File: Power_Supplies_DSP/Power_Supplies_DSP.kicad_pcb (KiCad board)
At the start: 4 copper layers, 149.3 x 91.8 mm, 54 parts, among them J22 USB_C_Receptacle_USB2.0, J28 PINHD_1x2_Female, J34 PINHD_1x1_Female, J35 PINHD_1x1_Female, J37 PINHD_1x3_Female, J41 PINHD_1x10_Female, J8 FTSH-110-01-F-DV-K, U12 XU316-1024-TQ128-I24, U13 Si5351A-B-GT, U14 W25Q64JVSSIQ (FLASH MEMORY), U37 PEC11R-4030F-N0024, X1 FA-238 24.0000MB-C0 (CRYSTAL), X2 FA-238 24.0000MB-C0

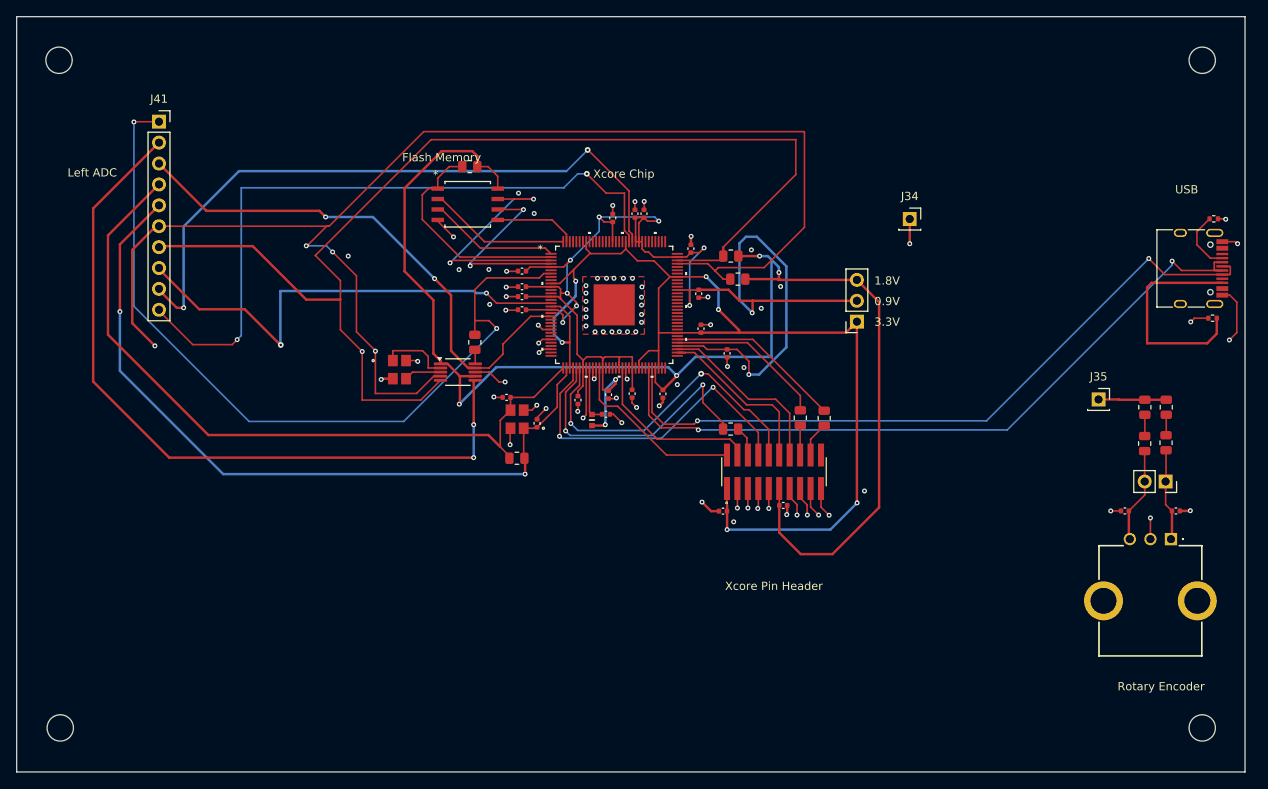
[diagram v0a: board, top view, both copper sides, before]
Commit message: mcu PCB
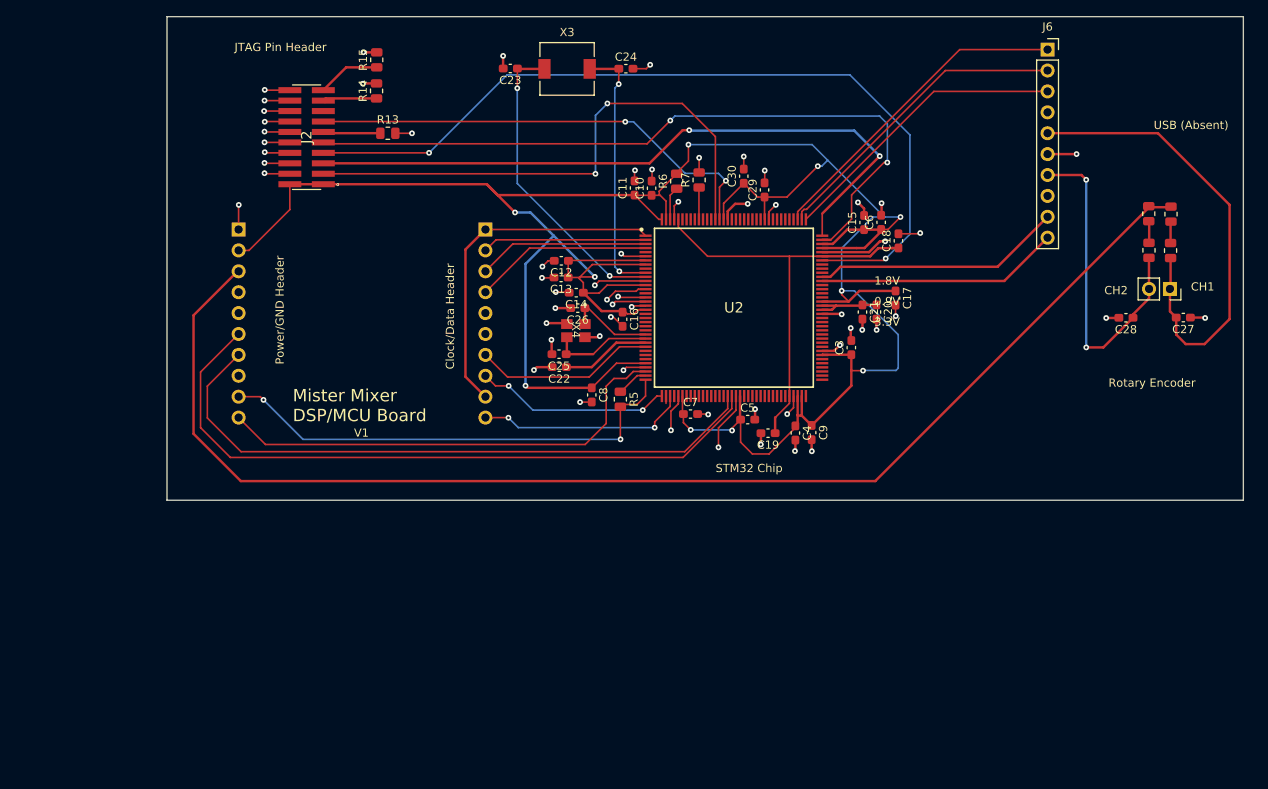
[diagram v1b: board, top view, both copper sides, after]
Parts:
- removed C202, C203, C204, C205, C207, C208, C209, C210, C211, C212, C213, C214, C215, C216, C217, C218: 100nF, Capacitor_SMD:C_0402_1005Metric
- removed C206: 2.2uF, Capacitor_SMD:C_0402_1005Metric
- removed C232: 1uF, Capacitor_SMD:C_0402_1005Metric
- removed C49, C50: 18pF, Capacitor_SMD:C_0402_1005Metric
- removed FL1: BLM18AG601SZ1D, SamacSys_Parts:BLM18SP221SN1B
- removed H1, H2, H3, H4: MountingHole_M3, MountingHole:MountingHole_3.2mm_M3
- removed J22: USB_C_Receptacle_USB2.0, Connector_USB:USB_C_Receptacle_HRO_TYPE-C-31-M-12
- removed J34, J35: PINHD_1x1_Female, Connector_PinSocket_2.54mm:PinSocket_1x01_P2.54mm_Vertical
- removed J37: PINHD_1x3_Female, Connector_PinSocket_2.54mm:PinSocket_1x03_P2.54mm_Vertical
- removed J41: PINHD_1x10_Female, Connector_PinSocket_2.54mm:PinSocket_1x10_P2.54mm_Vertical
- removed J8: FTSH-110-01-F-DV-K, SamacSys_Parts:FTSH-110-XX-YYY-DV-K
- removed R164: 0, Resistor_SMD:R_0805_2012Metric
- removed R165, R166: 43, Resistor_SMD:R_0805_2012Metric
- removed R174, R179: 5k1, Resistor_SMD:R_0402_1005Metric
- removed R34: 10K, Resistor_SMD:R_0805_2012Metric
- removed R35: 33, Resistor_SMD:R_0805_2012Metric
- removed R36: 1M, Resistor_SMD:R_0805_2012Metric
- removed R72, R73: 4.7K, Resistor_SMD:R_0805_2012Metric
- removed U12: XU316-1024-TQ128-I24, SamacSys_Parts:TQFP128_196X196_XMO
- removed U13: Si5351A-B-GT, Package_SO:MSOP-10_3x3mm_P0.5mm
- removed U14: W25Q64JVSSIQ (FLASH MEMORY), SamacSys_Parts:SOIC-8_5P28X5P28_WIN
- removed U37: PEC11R-4030F-N0024, SamacSys_Parts:PEC11R4030FN0024
- removed X1: FA-238 24.0000MB-C0 (CRYSTAL), SamacSys_Parts:FA-238_EPS
- removed X2: FA-238 24.0000MB-C0, SamacSys_Parts:FA-238_EPS
- added C10: 100nF, Capacitor_SMD:C_0603_1608Metric_Pad1.08x0.95mm_HandSolder, F.Cu at (201.4, 136.8)
- added C11: 100nF, Capacitor_SMD:C_0603_1608Metric_Pad1.08x0.95mm_HandSolder, F.Cu at (199.3, 136.7)
- added C12: 100nF, Capacitor_SMD:C_0603_1608Metric_Pad1.08x0.95mm_HandSolder, F.Cu at (190.4, 145.6)
- added C13: 100nF, Capacitor_SMD:C_0603_1608Metric_Pad1.08x0.95mm_HandSolder, F.Cu at (190.4, 147.6)
- added C14: 4.7 uF, Capacitor_SMD:C_0603_1608Metric_Pad1.08x0.95mm_HandSolder, F.Cu at (192.2, 149.4)
- added C15: 100nF, Capacitor_SMD:C_0603_1608Metric_Pad1.08x0.95mm_HandSolder, F.Cu at (227.2, 140.9)
- added C16: 100nF, Capacitor_SMD:C_0603_1608Metric_Pad1.08x0.95mm_HandSolder, F.Cu at (197.8, 152.7)
- added C17: 4.7uF, Capacitor_SMD:C_0603_1608Metric_Pad1.08x0.95mm_HandSolder, F.Cu at (231.0, 150.1)
- added C18: 2.2uF, Capacitor_SMD:C_0603_1608Metric_Pad1.08x0.95mm_HandSolder, F.Cu at (231.4, 143.2)
- added C19: 2.2uF, Capacitor_SMD:C_0603_1608Metric_Pad1.08x0.95mm_HandSolder, F.Cu at (215.5, 166.5)
- added C20: 1uF, Capacitor_SMD:C_0603_1608Metric_Pad1.08x0.95mm_HandSolder, F.Cu at (228.7, 151.8)
- added C21: 100nF, Capacitor_SMD:C_0603_1608Metric_Pad1.08x0.95mm_HandSolder, F.Cu at (227.0, 151.8)
- added C22: 100nF, Capacitor_SMD:C_0603_1608Metric_Pad1.08x0.95mm_HandSolder, F.Cu at (190.2, 158.5)
- added C23: 12pF, Capacitor_SMD:C_0603_1608Metric_Pad1.08x0.95mm_HandSolder, F.Cu at (184.2, 122.2)
- added C24: 12pF, Capacitor_SMD:C_0603_1608Metric_Pad1.08x0.95mm_HandSolder, F.Cu at (198.2, 122.2)
- added C25: 10pF, Capacitor_SMD:C_0603_1608Metric_Pad1.08x0.95mm_HandSolder, F.Cu at (190.1, 156.9)
- added C26: 10pF, Capacitor_SMD:C_0603_1608Metric_Pad1.08x0.95mm_HandSolder, F.Cu at (192.4, 151.3)
- added C29: 100nF, Capacitor_SMD:C_0603_1608Metric_Pad1.08x0.95mm_HandSolder, F.Cu at (215.1, 137.0)
- added C3: 100nF, Capacitor_SMD:C_0603_1608Metric_Pad1.08x0.95mm_HandSolder, F.Cu at (225.7, 156.1)
- added C30: 100nF, Capacitor_SMD:C_0603_1608Metric_Pad1.08x0.95mm_HandSolder, F.Cu at (212.6, 135.3)
- added C4: 100nF, Capacitor_SMD:C_0603_1608Metric_Pad1.08x0.95mm_HandSolder, F.Cu at (218.8, 166.5)
- added C5: 100nF, Capacitor_SMD:C_0603_1608Metric_Pad1.08x0.95mm_HandSolder, F.Cu at (213.1, 164.9)
- added C6: 100nF, Capacitor_SMD:C_0603_1608Metric_Pad1.08x0.95mm_HandSolder, F.Cu at (229.3, 140.9)
- added C7: 100nF, Capacitor_SMD:C_0603_1608Metric_Pad1.08x0.95mm_HandSolder, F.Cu at (206.1, 164.2)
- added C8: 100nF, Capacitor_SMD:C_0603_1608Metric_Pad1.08x0.95mm_HandSolder, F.Cu at (194.1, 161.9)
- added C9: 100nF, Capacitor_SMD:C_0603_1608Metric_Pad1.08x0.95mm_HandSolder, F.Cu at (220.8, 166.4)
- added J1: PINHD_1x10_Male, Connector_PinHeader_2.54mm:PinHeader_1x10_P2.54mm_Vertical, B.Cu at (151.2, 141.8)
- added J2: SBH11-PBPC-D10-ST-BK, SamacSys_Parts:FTSH-110-XX-YYY-DV-K, F.Cu at (159.4, 130.6)
- added J4: PINHD_1x10_Male, Connector_PinHeader_2.54mm:PinHeader_1x10_P2.54mm_Vertical, B.Cu at (181.2, 141.8)
- added J6: PINHD_1x10_Female, Connector_PinSocket_2.54mm:PinSocket_1x10_P2.54mm_Vertical, F.Cu at (249.5, 119.9)
- added R13: 10k, Resistor_SMD:R_0805_2012Metric, F.Cu at (169.3, 130.1)
- added R14: 10k, Resistor_SMD:R_0805_2012Metric, F.Cu at (167.9, 124.9)
- added R15: 10k, Resistor_SMD:R_0805_2012Metric, F.Cu at (168.0, 121.2)
- added R5: 47, Resistor_SMD:R_0805_2012Metric, F.Cu at (197.6, 162.4)
- added R6: 10k, Resistor_SMD:R_0805_2012Metric, F.Cu at (204.4, 135.9)
- added R7: 10k, Resistor_SMD:R_0805_2012Metric, F.Cu at (207.2, 135.8)
- added U2: STM32H755ZIT6, SamacSys_Parts:QFP50P2200X2200X160-144N, F.Cu at (211.4, 151.3)
- added X3: NX3215SA-32.768K, Inductor_SMD:L_6.3x6.3_H3, F.Cu at (191.1, 122.2)
- added X4: NX2016SA-32MHZ, SamacSys_Parts:FA-238_EPS, F.Cu at (192.2, 154.1)
- C27: renamed from C235; footprint Capacitor_SMD:C_0402_1005Metric -> Capacitor_SMD:C_0603_1608Metric_Pad1.08x0.95mm_HandSolder
- C28: renamed from C234; footprint Capacitor_SMD:C_0402_1005Metric -> Capacitor_SMD:C_0603_1608Metric_Pad1.08x0.95mm_HandSolder
- moved R10 27.9 mm to (261.8, 139.8)
- moved C27 24.6 mm to (266.0, 152.5)
- moved C28 24.3 mm to (259.0, 152.5)
- moved R8 23.7 mm to (264.5, 139.9)
- moved R11 23.5 mm to (261.8, 144.3)
- moved J5 23.4 mm to (264.4, 149.0)
- moved R9 19.1 mm to (264.4, 144.3)
- renumbered J28 to J5, R178 to R10, R177 to R11, R176 to R8, R175 to R9
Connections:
- C27 pad 1: Net-(U37-CHANNEL_2) -> GND
- C27 pad 2: GND -> CHANNEL_1
- C28 pad 1: GND -> CHANNEL_2
- C28 pad 2: Net-(U37-CHANNEL_1) -> GND
- J5 pad 1: Net-(U37-CHANNEL_1) -> CHANNEL_1
- J5 pad 2: Net-(U37-CHANNEL_2) -> CHANNEL_2
- R10 pad 1: Net-(R176-Pad2) -> 5V
- R10 pad 2: Net-(U37-CHANNEL_2) -> Net-(R10-Pad2)
- R11 pad 1: Net-(R175-Pad2) -> Net-(R10-Pad2)
- R11 pad 2: Net-(U37-CHANNEL_1) -> CHANNEL_2
- R8 pad 2: Net-(R176-Pad2) -> Net-(R8-Pad2)
- R9 pad 1: 5V -> Net-(R8-Pad2)
- R9 pad 2: Net-(R175-Pad2) -> CHANNEL_1
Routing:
- net 0.9V: track 185.3 -> 0.00 mm, vias 12 -> 0
- net SCL: track 167.2 -> 0.00 mm, vias 4 -> 0
- net 3.3V: track 177.3 -> 328.5 mm, vias 4 -> 10
- net 5V: track 8.24 -> 157.0 mm
- net SDA: track 144.1 -> 0.00 mm, vias 1 -> 0
- net 1.8V: track 137.6 -> 0.00 mm, vias 6 -> 0
- net SWDIO: track 0.00 -> 102.3 mm, vias 0 -> 2
- net MCLK: track 98.7 -> 0.00 mm, vias 2 -> 0
- net XIN: track 92.4 -> 0.00 mm, vias 2 -> 0
- net BCK: track 91.9 -> 0.00 mm, vias 2 -> 0
- net XOUT: track 90.6 -> 0.00 mm
- net SWCLK: track 0.00 -> 88.6 mm, vias 0 -> 2
- net USB_DN: track 88.4 -> 0.00 mm, vias 2 -> 0
- net USB_DP: track 87.3 -> 0.00 mm, vias 2 -> 0
- net DATA_OUT_2: track 84.9 -> 0.00 mm, vias 2 -> 0
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- removed copper zone on F.Cu, net GND
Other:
- board size 149.3 x 91.8 mm -> 130.8 x 58.8 mm
- board text added: "CH1"
- board text added: "CH2"
- board text added: "Clock/Data Header"
- board text added: "JTAG Pin Header"
- board text added: "Mister Mixer DSP/MCU Board"
- board text added: "Power/GND Header"
- board text added: "STM32 Chip"
- board text added: "USB (Absent)"
- board text added: "V1"
- board text removed: "Flash Memory"
- board text removed: "Left ADC"
- board text removed: "USB"
- board text removed: "Xcore Chip"
- board text removed: "Xcore Pin Header"

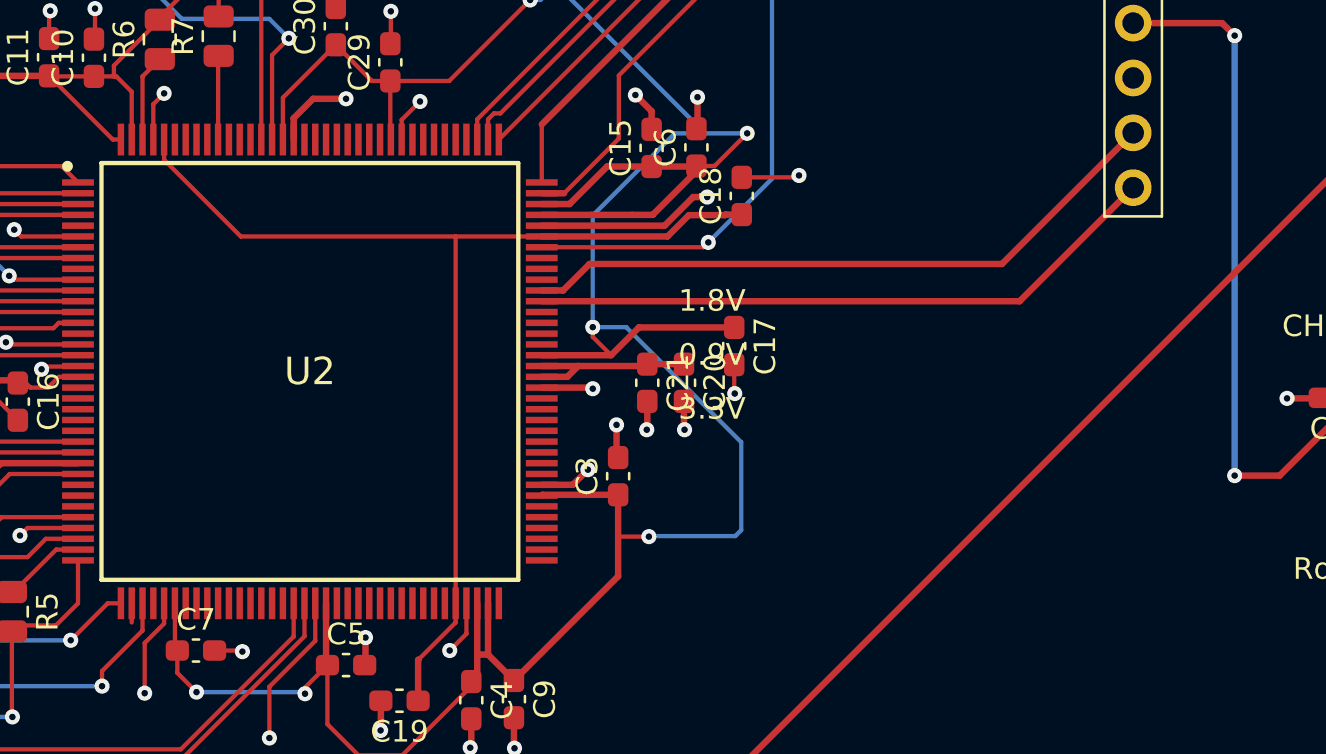
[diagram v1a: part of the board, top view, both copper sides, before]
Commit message: fixed pcb conexions
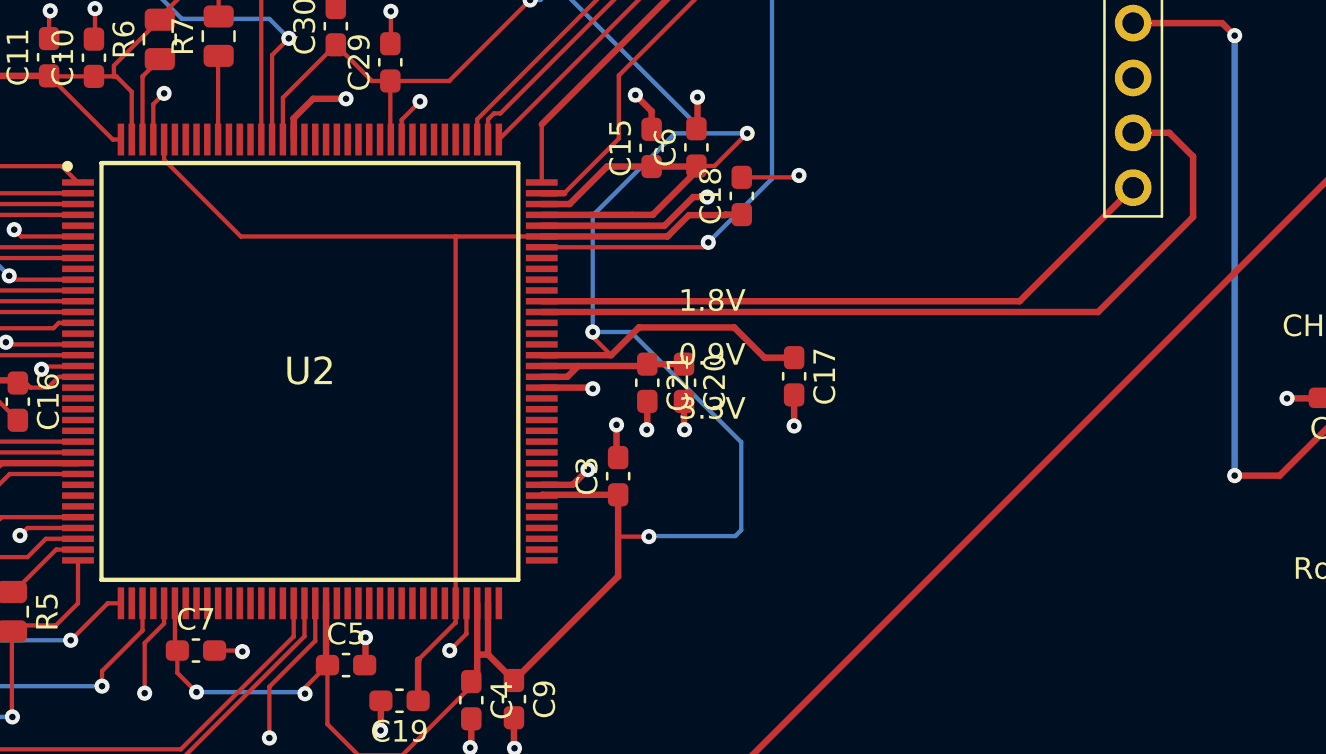
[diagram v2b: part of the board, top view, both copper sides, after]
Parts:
- moved C17 3.11 mm to (233.8, 151.5)
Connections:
- J4 pad 9: SAI1_MCLK_A -> SAI2_MCLK_B
- U2 pad 38: SAI2_MCLK_B -> unconnected-(U2A-PA1-Pad38)
- U2 pad 96: unconnected-(U2A-PC9-Pad96) -> I2C3_SDA
- U2 pad 98: I2C3_SDA -> unconnected-(U2A-PA9-Pad98)
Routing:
- net I2C3_SDA: track 30.4 -> 38.0 mm
- net 3.3V: track 328.5 -> 331.8 mm
- net SAI2_MCLK_B: track 0.89 -> 0.00 mm

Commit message: added changes that weeks wanted 🐷
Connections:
- J1 pad 10: AGND -> unconnected-(J1-Pad10)
- U2 pad 34: AGND -> GND
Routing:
- net AGND: track 57.1 -> 0.00 mm
- net GND: track 153.5 -> 156.0 mm, vias 61 -> 62
